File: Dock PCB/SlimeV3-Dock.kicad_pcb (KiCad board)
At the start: 2 copper layers, 17.8 x 24.3 mm, 4 parts, among them J1 DNP, J2 DNP, U1 DNP, U2 YTC-TC16S-128

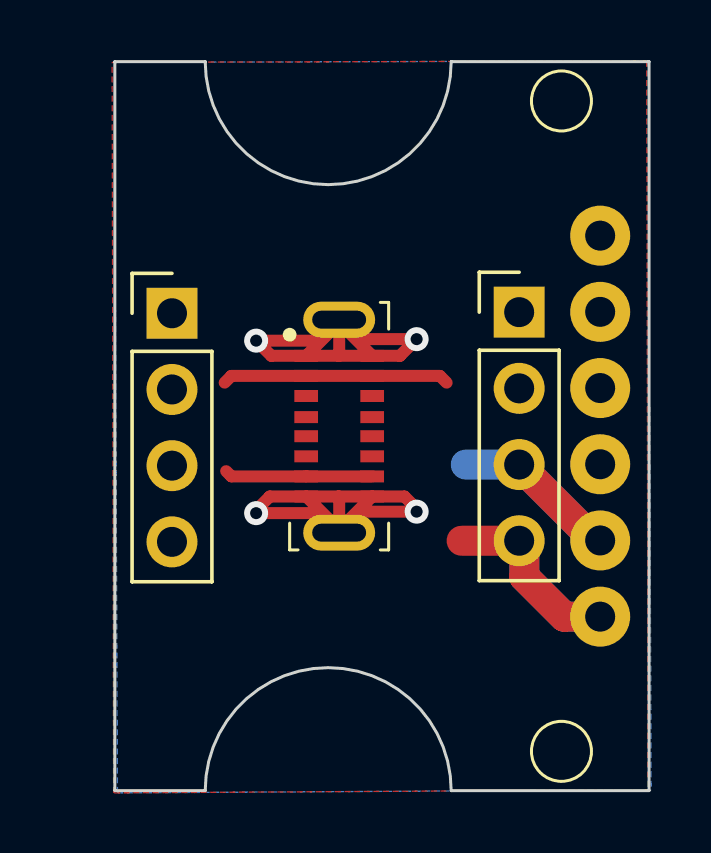
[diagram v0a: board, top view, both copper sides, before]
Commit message: Added pin jig. Did not modify PCB, only opened for reference.
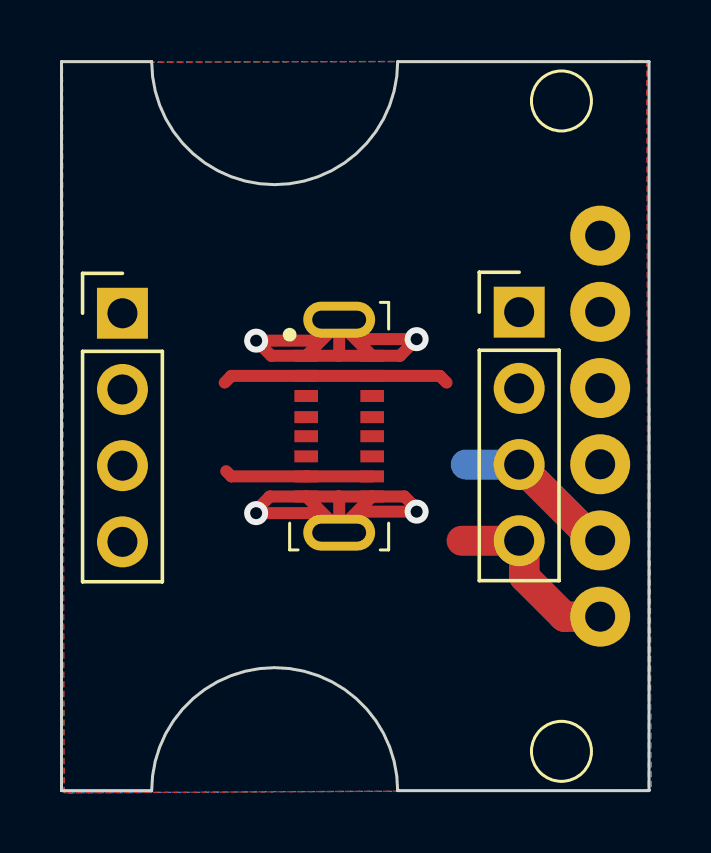
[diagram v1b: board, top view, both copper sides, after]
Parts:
- moved J2 1.65 mm to (150.9, 89.0)
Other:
- board size 17.8 x 24.3 mm -> 19.6 x 24.3 mm
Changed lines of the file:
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@@
 	(footprint "Connector_PinHeader_2.54mm:PinHeader_1x04_P2.54mm_Vertical"
 		(layer "F.Cu")
-		(at 152.527 89.037)
+		(at 150.876 89.037)
 		(descr "Through hole straight pin header, 1x04, 2.54mm pitch, single row")
 		(tags "Through hole pin header THT 1x04 2.54mm single row")
@@
 	)
 	(gr_line
-		(start 150.622 104.95)
-		(end 150.622 80.65)
+		(start 148.844 104.95)
+		(end 148.844 80.65)
 		(stroke
 			(width 0.1)
@@
 	(gr_line
 		(start 168.428954 104.95)
-		(end 161.834 104.95)
+		(end 160.05 104.95)
 		(stroke
 			(width 0.1)
@@
 	)
 	(gr_line
-		(start 161.834 80.65)
+		(start 160.05 80.65)
 		(end 168.428954 80.65)
 		(stroke
@@
 	)
 	(gr_arc
-		(start 153.634 104.95)
-		(mid 157.734 100.85)
-		(end 161.834 104.95)
+		(start 151.85 104.95)
+		(mid 155.95 100.85)
+		(end 160.05 104.95)
 		(stroke
 			(width 0.1)
@@
 	)
 	(gr_line
-		(start 150.622 80.65)
-		(end 153.634 80.65)
+		(start 148.844 80.65)
+		(end 151.85 80.65)
 		(stroke
 			(width 0.1)
@@
 	)
 	(gr_arc
-		(start 161.834 80.65)
-		(mid 157.734 84.75)
-		(end 153.634 80.65)
+		(start 160.05 80.65)
+		(mid 155.95 84.75)
+		(end 151.85 80.65)
 		(stroke
 			(width 0.1)
@@
 	)
 	(gr_line
-		(start 153.634 104.95)
-		(end 150.622 104.95)
+		(start 151.85 104.95)
+		(end 148.844 104.95)
 		(stroke
 			(width 0.1)
@@
 		(polygon
 			(pts
-				(xy 150.532 80.674294) (xy 168.35 80.624294) (xy 168.4 104.924294) (xy 150.582 105.024294)
+				(xy 148.881 80.674294) (xy 168.35 80.624294) (xy 168.4 104.924294) (xy 148.931 105.024294)
 			)
 		)
@@
 		(polygon
 			(pts
-				(xy 150.609 80.674294) (xy 168.4 80.624294) (xy 168.5 104.924294) (xy 150.709 105.024294)
-			)
-		)
+				(xy 148.831 80.674294) (xy 168.4 80.624294) (xy 168.5 104.924294) (xy 148.931 105.024294)
+			)
+		)

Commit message: - Added dimensions to dock pcb - some other stuff probably that i forgot to write down
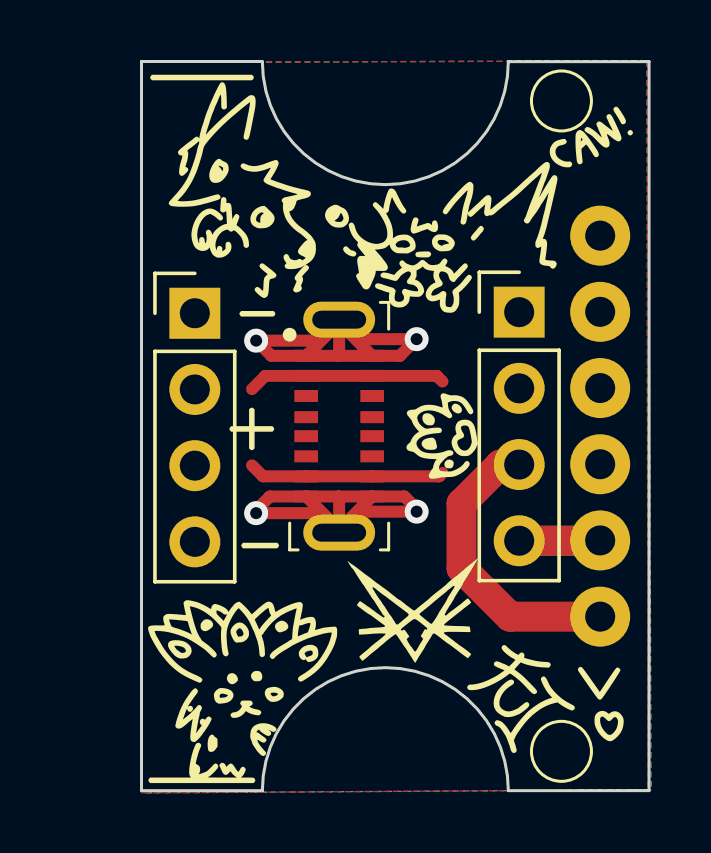
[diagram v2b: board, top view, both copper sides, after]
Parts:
- added G***: LOGO, LOGO, F.Cu at (160.0, 92.8)
- moved J2 2.41 mm to (153.3, 89.0)
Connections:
- J1 pad 3: GND -> VBUS
- J1 pad 4: VBUS -> GND
- J2 pad 3: GND -> VBUS
- J2 pad 4: VBUS -> GND
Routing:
- net GND: track 41.7 -> 38.2 mm
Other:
- board size 19.6 x 24.3 mm -> 16.9 x 24.3 mm
